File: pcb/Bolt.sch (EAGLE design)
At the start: 58 parts, among them J1 10118194-0001LF, Q1 XT60_YELLOW, Q2 MMSS8050-H-TP, Q3 MMSS8050-H-TP, U1 FT231XS-R, U2 ESP32-WROOM-32D, U3 LM1117DT-3.3/NOPB

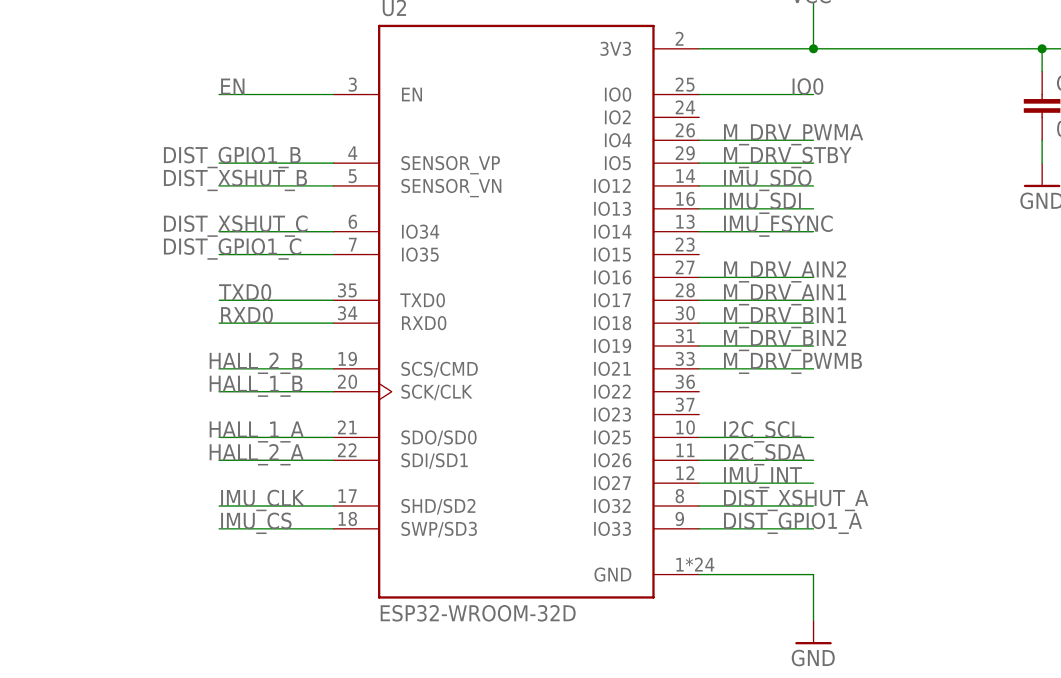
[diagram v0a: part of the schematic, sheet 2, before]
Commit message: Fixed XSHUT routes on PCB resulting in Bolt v1.1
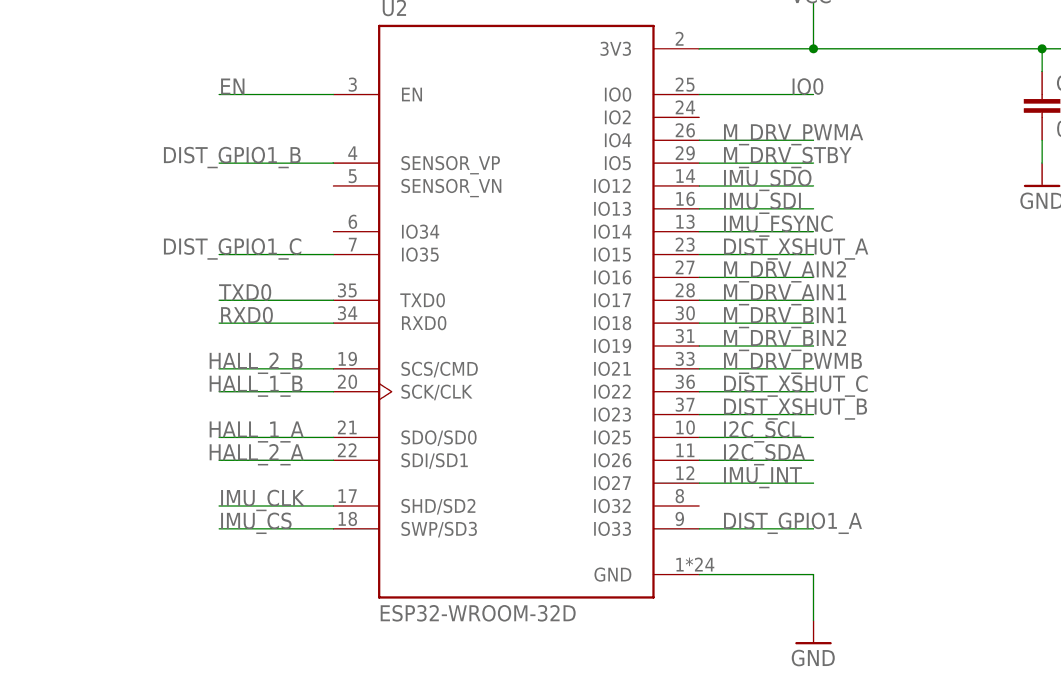
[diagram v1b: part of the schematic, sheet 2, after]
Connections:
- net DIST_XSHUT_A: now also U2.IO15; no longer U2.IO32
- net DIST_XSHUT_B: now also U2.IO23; no longer U2.SENSOR_VN
- net DIST_XSHUT_C: now also U2.IO22; no longer U2.IO34
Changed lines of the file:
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@@
 <net name="DIST_XSHUT_A" class="0">
 <segment>
-<wire x1="101.6" y1="60.96" x2="114.3" y2="60.96" width="0.1524" layer="91"/>
-<pinref part="U2" gate="G$1" pin="IO32"/>
-<label x="104.14" y="60.96" size="1.778" layer="95"/>
+<wire x1="101.6" y1="88.9" x2="114.3" y2="88.9" width="0.1524" layer="91"/>
+<pinref part="U2" gate="G$1" pin="IO15"/>
+<label x="104.14" y="88.9" size="1.778" layer="95"/>
 </segment>
 </net>
@@
 </segment>
 </net>
-<net name="DIST_XSHUT_B" class="0">
-<segment>
-<pinref part="U2" gate="G$1" pin="SENSOR_VN"/>
-<wire x1="60.96" y1="96.52" x2="48.26" y2="96.52" width="0.1524" layer="91"/>
-<label x="41.91" y="96.52" size="1.778" layer="95"/>
-</segment>
-</net>
 <net name="DIST_XSHUT_C" class="0">
 <segment>
-<wire x1="60.96" y1="91.44" x2="48.26" y2="91.44" width="0.1524" layer="91"/>
-<pinref part="U2" gate="G$1" pin="IO34"/>
-<label x="41.91" y="91.44" size="1.778" layer="95"/>
+<wire x1="114.3" y1="73.66" x2="101.6" y2="73.66" width="0.1524" layer="91"/>
+<pinref part="U2" gate="G$1" pin="IO22"/>
+<label x="104.14" y="73.66" size="1.778" layer="95"/>
 </segment>
 </net>
@@
 </segment>
 </net>
+<net name="DIST_XSHUT_B" class="0">
+<segment>
+<wire x1="101.6" y1="71.12" x2="114.3" y2="71.12" width="0.1524" layer="91"/>
+<pinref part="U2" gate="G$1" pin="IO23"/>
+<label x="104.14" y="71.12" size="1.778" layer="95"/>
+</segment>
+</net>
